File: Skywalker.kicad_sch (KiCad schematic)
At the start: 53 parts

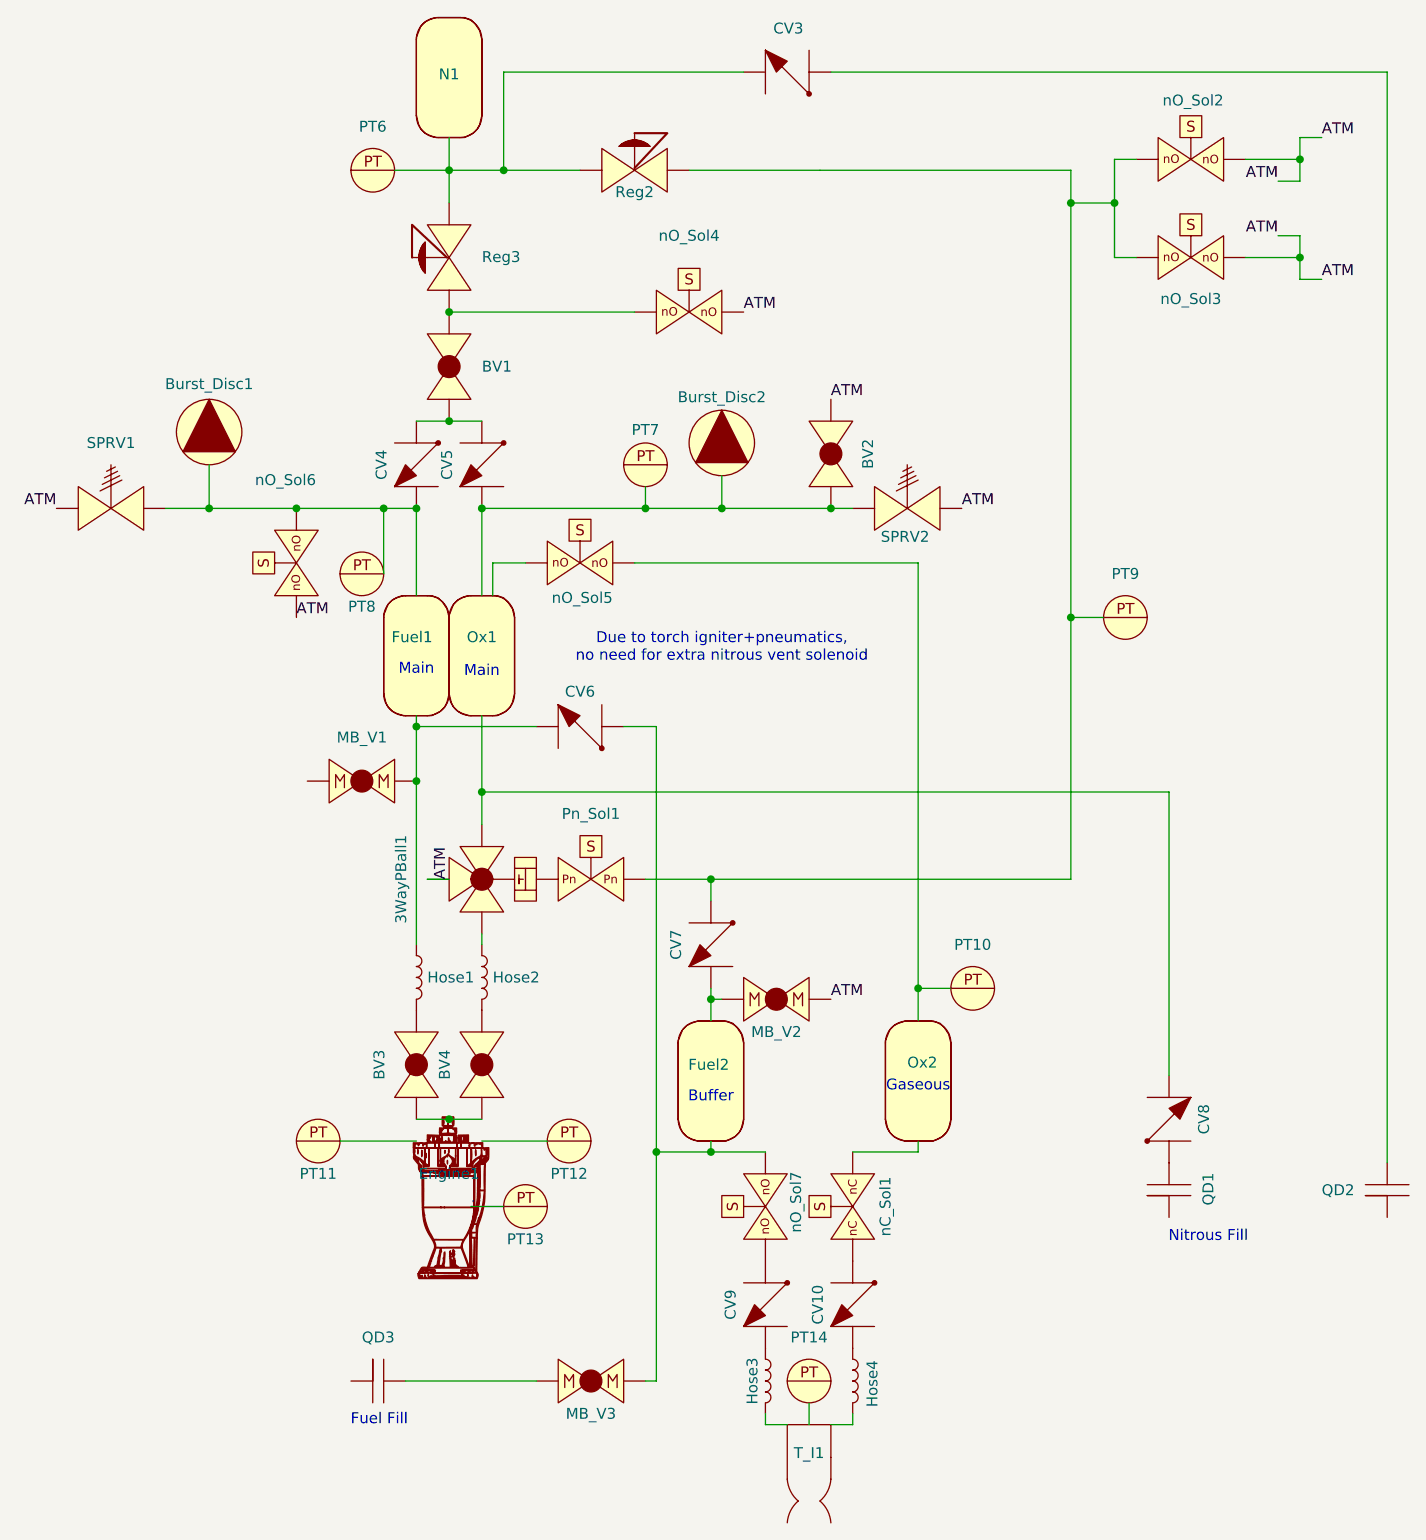
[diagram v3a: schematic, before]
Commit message: Added Igniter + Hopper Engine test
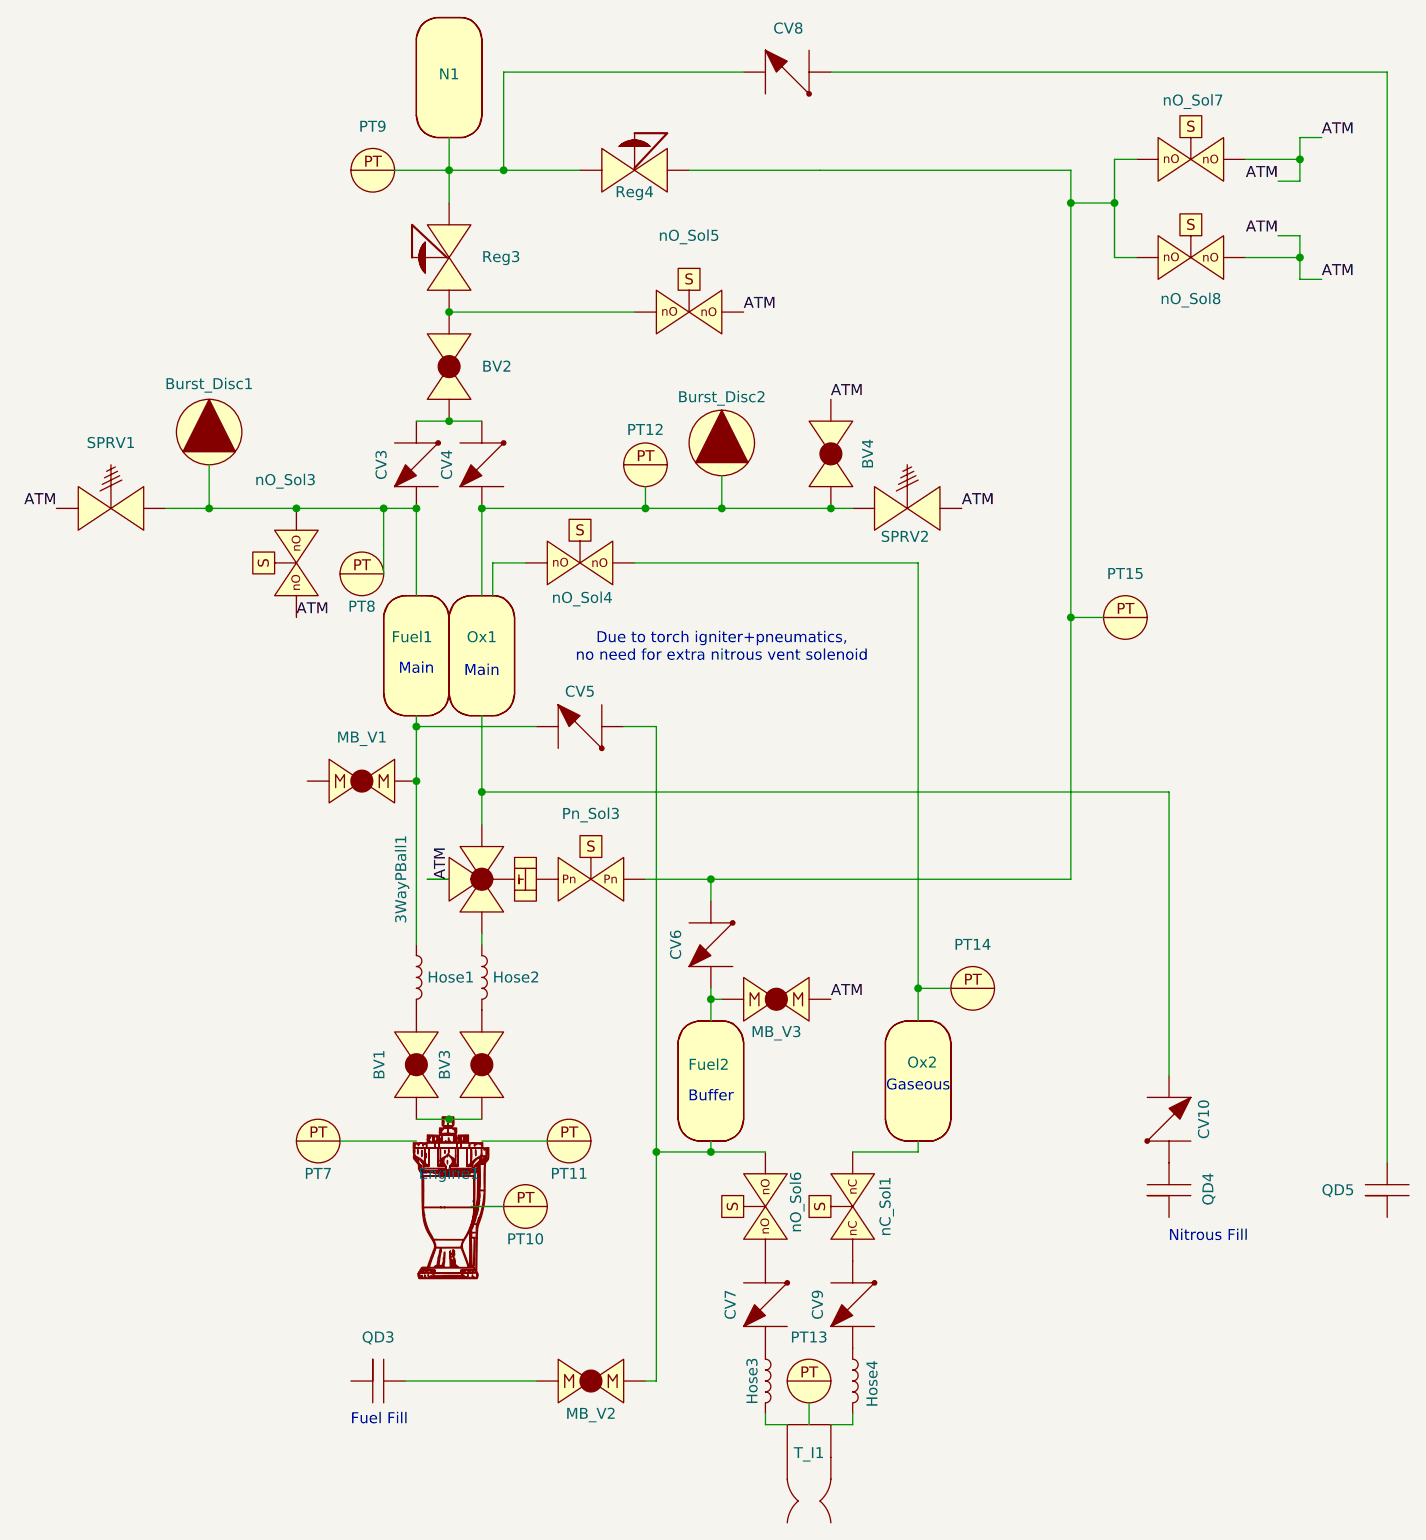
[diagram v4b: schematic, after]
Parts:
- renumbered BV3 to BV1, BV1 to BV2, BV4 to BV3, BV2 to BV4, CV8 to CV10, CV4 to CV3, CV5 to CV4, CV6 to CV5, CV7 to CV6, CV9 to CV7, CV3 to CV8, CV10 to CV9, MB_V3 to MB_V2, MB_V2 to MB_V3, PT13 to PT10, PT12 to PT11, PT7 to PT12, PT14 to PT13, PT10 to PT14, PT9 to PT15, PT11 to PT7, PT6 to PT9, Pn_Sol1 to Pn_Sol3, QD1 to QD4, QD2 to QD5, Reg2 to Reg4, nO_Sol6 to nO_Sol3, nO_Sol5 to nO_Sol4, nO_Sol4 to nO_Sol5, nO_Sol7 to nO_Sol6, nO_Sol2 to nO_Sol7, nO_Sol3 to nO_Sol8
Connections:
- net at N1.: now also CV8., PT9., Reg3., Reg4.
- net at Engine1.: now also PT7.; no longer PT11.
- net at PT7.: no longer Engine1.
- net at CV9.: now also Hose4.1; no longer nC_Sol1.
- net at QD4.: now also CV10.
- new net: CV6., PT15., Pn_Sol3., Reg4., nO_Sol7., nO_Sol8.
- new net: CV6., Fuel2., MB_V3.
- new net: Engine1., PT11.
- new net: BV1., BV3., Engine1.
- new net: CV5., Fuel2., MB_V2., nO_Sol6.
- new net: CV9., nC_Sol1.
- new net: Burst_Disc1., CV3., Fuel1., PT8., SPRV1., nO_Sol3.
- new net: BV2., CV3., CV4.
- new net: Ox2., PT14., nO_Sol4.
- new net: 3WayPBall1., CV10., Ox1.
- new net: BV4., Burst_Disc2., CV4., Ox1., PT12., SPRV2.
- now unconnected: Burst_Disc1., Burst_Disc2., PT12., PT14., PT15., PT8., PT9.

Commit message: overwrite
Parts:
- renumbered PT10 to Chamber, PT7 to Fuel_Inj, PT13 to Igniter, PT9 to N2_Hose, PT11 to Ox_Inj
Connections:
- net at N1.: now also CV8., N2_Hose., Reg3., Reg4.
- net at Engine1.: now also Fuel_Inj.; no longer Ox_Inj.
- net at Fuel_Inj.: no longer Engine1.
- net at CV9.: now also Hose4.1; no longer nC_Sol1.
- net N2_GSS: now reaches QD5.
- net OX_GSS: now reaches QD4.
- new net: CV6., PT15., Pn_Sol3., Reg4., nO_Sol7., nO_Sol8.
- new net: CV6., Fuel2., MB_V3.
- new net: Engine1., Ox_Inj.
- new net: BV1., BV3., Engine1.
- new net: CV5., Fuel2., MB_V2., nO_Sol6.
- new net: CV9., nC_Sol1.
- new net: Burst_Disc1., CV3., Fuel1., PT8., SPRV1., nO_Sol3.
- new net: BV2., CV3., CV4.
- new net: Ox2., PT14., nO_Sol4.
- new net: 3WayPBall1., CV10., Ox1.
- new net: BV4., Burst_Disc2., CV4., Ox1., PT12., SPRV2.
- now unconnected: Burst_Disc1., Burst_Disc2., N2_Hose., PT12., PT14., PT15., PT8.
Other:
- note removed: "Nitrous Fill"
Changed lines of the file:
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@@
+	(wire
+		(pts
+			(xy 147.32 161.29) (xy 147.32 156.21)
+		)
+		(stroke
+			(width 0)
+			(type default)
+		)
+	)
 	(wire
 		(pts
@@
 	(wire
 		(pts
+			(xy 172.72 161.29) (xy 172.72 156.21)
+		)
+		(stroke
+			(width 0)
+			(type default)
+		)
+	)
+	(wire
+		(pts
 			(xy 140.97 33.02) (xy 140.97 38.1)
 		)
@@
 		)
 	)
-	(text "Nitrous Fill"
-		(exclude_from_sim no)
-		(at 151.892 158.496 0)
-		(effects
-			(font
-				(size 1.27 1.27)
-			)
-		)
-	)
 	(text "Gaseous"
 		(exclude_from_sim no)
@@
 	(label "ATM"
 		(at 17.78 73.66 180)
+		(fields_autoplaced yes)
 		(effects
 			(font
@@
 	(label "ATM"
 		(at 160.02 41.91 180)
+		(fields_autoplaced yes)
 		(effects
 			(font
@@
 	(label "ATM"
 		(at 165.1 46.99 0)
+		(fields_autoplaced yes)
 		(effects
 			(font
@@
 	(label "ATM"
 		(at 123.19 73.66 0)
+		(fields_autoplaced yes)
 		(effects
 			(font
@@
 	(label "."
 		(at 66.04 154.94 0)
+		(fields_autoplaced yes)
 		(effects
 			(font
@@
 	(label "ATM"
 		(at 107.95 130.81 0)
+		(fields_autoplaced yes)
 		(effects
 			(font
@@
 		)
 	)
-	(label "ATM"
-		(at 165.1 30.48 0)
+	(label "N2_GSS"
+		(at 172.72 161.29 180)
+		(fields_autoplaced yes)
 		(effects
 			(font
 				(size 1.27 1.27)
 			)
+			(justify right bottom)
+		)
+	)
+	(label "ATM"
+		(at 165.1 30.48 0)
+		(fields_autoplaced yes)
+		(effects
+			(font
+				(size 1.27 1.27)
+			)
 			(justify left bottom)
 		)
@@
 	(label "."
 		(at 105.41 180.34 0)
+		(fields_autoplaced yes)
 		(effects
 			(font
@@
 		)
 	)
+	(label "OX_GSS"
+		(at 147.32 161.29 0)
+		(fields_autoplaced yes)
+		(effects
+			(font
+				(size 1.27 1.27)
+			)
+			(justify left bottom)
+		)
+	)
 	(label "."
 		(at 68.58 83.82 0)
+		(fields_autoplaced yes)
 		(effects
 			(font
@@
 	(label "ATM"
 		(at 97.79 50.8 0)
+		(fields_autoplaced yes)
 		(effects
 			(font
@@
 	(label "ATM"
 		(at 63.5 116.84 90)
+		(fields_autoplaced yes)
 		(effects
 			(font
@@
 	(label "ATM"
 		(at 45.72 86.36 0)
+		(fields_autoplaced yes)
 		(effects
 			(font
@@
 	(label "ATM"
 		(at 107.95 60.96 0)
+		(fields_autoplaced yes)
 		(effects
 			(font
@@
 	(label "ATM"
 		(at 160.02 35.56 180)
+		(fields_autoplaced yes)
 		(effects
 			(font
@@
 	)
 	(symbol
+		(lib_name "PID_symbols:Pressure_Transducer")
 		(lib_id "PID_symbols:Pressure_Transducer")
 		(at 72.39 154.94 0)
@@
 		(on_board yes)
 		(dnp no)
-		(property "Reference" "PT10"
+		(property "Reference" "Chamber"
 			(at 72.39 158.75 0)
 			(effects
@@
 			(project "P_IDs"
 				(path "/045f1f05-3134-4b6d-91b6-463031104f1e/8ff5724e-b29b-49c2-a1fa-190081404476"
-					(reference "PT10")
+					(reference "Chamber")
 					(unit 1)
 				)
@@
 	)
 	(symbol
+		(lib_name "PID_symbols:Pressure_Transducer")
 		(lib_id "PID_symbols:Pressure_Transducer")
 		(at 77.47 147.32 0)
@@
 		(on_board yes)
 		(dnp no)
-		(property "Reference" "PT11"
+		(property "Reference" "Ox_Inj"
 			(at 77.47 151.13 0)
 			(effects
@@
 			(project "P_IDs"
 				(path "/045f1f05-3134-4b6d-91b6-463031104f1e/8ff5724e-b29b-49c2-a1fa-190081404476"
-					(reference "PT11")
+					(reference "Ox_Inj")
 					(unit 1)
 				)
@@
 	)
 	(symbol
+		(lib_name "PID_symbols:Pressure_Transducer")
 		(lib_id "PID_symbols:Pressure_Transducer")
 		(at 48.26 147.32 0)
@@
 		(on_board yes)
 		(dnp no)
-		(property "Reference" "PT7"
+		(property "Reference" "Fuel_Inj"
 			(at 48.26 151.13 0)
 			(effects
@@
 			(project "P_IDs"
 				(path "/045f1f05-3134-4b6d-91b6-463031104f1e/8ff5724e-b29b-49c2-a1fa-190081404476"
-					(reference "PT7")
+					(reference "Fuel_Inj")
 					(unit 1)
 				)
@@
 	)
 	(symbol
+		(lib_name "PID_symbols:Pressure_Transducer")
 		(lib_id "PID_symbols:Pressure_Transducer")
 		(at 105.41 175.26 0)
@@
 		(dnp no)
 		(fields_autoplaced yes)
-		(property "Reference" "PT13"
+		(property "Reference" "Igniter"
 			(at 105.41 170.18 0)
 			(effects
@@
 			(project ""
 				(path "/045f1f05-3134-4b6d-91b6-463031104f1e/8ff5724e-b29b-49c2-a1fa-190081404476"
-					(reference "PT13")
+					(reference "Igniter")
 					(unit 1)
 				)
@@
 	)
 	(symbol
+		(lib_name "PID_symbols:Pressure_Transducer")
 		(lib_id "PID_symbols:Pressure_Transducer")
 		(at 54.61 34.29 0)
@@
 		(dnp no)
 		(fields_autoplaced yes)
-		(property "Reference" "PT9"
+		(property "Reference" "N2_Hose"
 			(at 54.61 29.21 0)
 			(effects
@@
 			(project ""
 				(path "/045f1f05-3134-4b6d-91b6-463031104f1e/8ff5724e-b29b-49c2-a1fa-190081404476"
-					(reference "PT9")
-					(unit 1)
-				)
+					(reference "N2_Hose")
+					(unit 1)
+				)

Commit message: no message
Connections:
- net at N1.: now also CV8., N2_Hose., Reg3., Reg4.
- net at Engine1.: now also Fuel_Inj.; no longer Ox_Inj.
- net at Fuel_Inj.: no longer Engine1.
- net at CV9.: now also Hose4.1; no longer nC_Sol1.
- new net: CV6., PT15., Pn_Sol3., Reg4., nO_Sol7., nO_Sol8.
- new net: CV6., Fuel2., MB_V3.
- new net: Engine1., Ox_Inj.
- new net: BV1., BV3., Engine1.
- new net: CV5., Fuel2., MB_V2., nO_Sol6.
- new net: CV9., nC_Sol1.
- new net: Burst_Disc1., CV3., Fuel1., PT8., SPRV1., nO_Sol3.
- new net: BV2., CV3., CV4.
- new net: Ox2., PT14., nO_Sol4.
- new net: 3WayPBall1., CV10., Ox1.
- new net: BV4., Burst_Disc2., CV4., Ox1., PT12., SPRV2.
- now unconnected: Burst_Disc1., Burst_Disc2., N2_Hose., PT12., PT14., PT15., PT8.
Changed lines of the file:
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@@
 	)
 	(symbol
-		(lib_name "PID_symbols:Pressure_Transducer")
 		(lib_id "PID_symbols:Pressure_Transducer")
 		(at 72.39 154.94 0)
@@
 	)
 	(symbol
-		(lib_name "PID_symbols:Pressure_Transducer")
 		(lib_id "PID_symbols:Pressure_Transducer")
 		(at 77.47 147.32 0)
@@
 	)
 	(symbol
-		(lib_name "PID_symbols:Pressure_Transducer")
 		(lib_id "PID_symbols:Pressure_Transducer")
 		(at 48.26 147.32 0)
@@
 	)
 	(symbol
-		(lib_name "PID_symbols:Pressure_Transducer")
 		(lib_id "PID_symbols:Pressure_Transducer")
 		(at 105.41 175.26 0)
@@
 	)
 	(symbol
-		(lib_name "PID_symbols:Pressure_Transducer")
 		(lib_id "PID_symbols:Pressure_Transducer")
 		(at 54.61 34.29 0)
@@
 		)
 	)
+	(sheet_instances
+		(path "/"
+			(page "1")
+		)
+	)

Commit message: no message
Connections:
- net at N1.: now also CV8., N2_Hose., Reg3., Reg4.
- net at Engine1.: now also Fuel_Inj.; no longer Ox_Inj.
- net at Fuel_Inj.: no longer Engine1.
- net at CV9.: now also Hose4.1; no longer nC_Sol1.
- new net: CV6., PT15., Pn_Sol3., Reg4., nO_Sol7., nO_Sol8.
- new net: CV6., Fuel2., MB_V3.
- new net: Engine1., Ox_Inj.
- new net: BV1., BV3., Engine1.
- new net: CV5., Fuel2., MB_V2., nO_Sol6.
- new net: CV9., nC_Sol1.
- new net: Burst_Disc1., CV3., Fuel1., PT8., SPRV1., nO_Sol3.
- new net: BV2., CV3., CV4.
- new net: Ox2., PT14., nO_Sol4.
- new net: 3WayPBall1., CV10., Ox1.
- new net: BV4., Burst_Disc2., CV4., Ox1., PT12., SPRV2.
- now unconnected: Burst_Disc1., Burst_Disc2., N2_Hose., PT12., PT14., PT15., PT8.
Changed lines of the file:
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@@
 	)
 	(symbol
+		(lib_name "PID_symbols:Pressure_Transducer")
 		(lib_id "PID_symbols:Pressure_Transducer")
 		(at 72.39 154.94 0)
@@
 	)
 	(symbol
+		(lib_name "PID_symbols:Pressure_Transducer")
 		(lib_id "PID_symbols:Pressure_Transducer")
 		(at 77.47 147.32 0)
@@
 	)
 	(symbol
+		(lib_name "PID_symbols:Pressure_Transducer")
 		(lib_id "PID_symbols:Pressure_Transducer")
 		(at 48.26 147.32 0)
@@
 	)
 	(symbol
+		(lib_name "PID_symbols:Pressure_Transducer")
 		(lib_id "PID_symbols:Pressure_Transducer")
 		(at 105.41 175.26 0)
@@
 	)
 	(symbol
+		(lib_name "PID_symbols:Pressure_Transducer")
 		(lib_id "PID_symbols:Pressure_Transducer")
 		(at 54.61 34.29 0)
@@
 		)
 	)
-	(sheet_instances
-		(path "/"
-			(page "1")
-		)
-	)

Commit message: no message
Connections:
- net at N1.: now also CV8., N2_Hose., Reg3., Reg4.
- net at Engine1.: now also Fuel_Inj.; no longer Ox_Inj.
- net at Fuel_Inj.: no longer Engine1.
- net at CV9.: now also Hose4.1; no longer nC_Sol1.
- new net: CV6., PT15., Pn_Sol3., Reg4., nO_Sol7., nO_Sol8.
- new net: CV6., Fuel2., MB_V3.
- new net: Engine1., Ox_Inj.
- new net: BV1., BV3., Engine1.
- new net: CV5., Fuel2., MB_V2., nO_Sol6.
- new net: CV9., nC_Sol1.
- new net: Burst_Disc1., CV3., Fuel1., PT8., SPRV1., nO_Sol3.
- new net: BV2., CV3., CV4.
- new net: Ox2., PT14., nO_Sol4.
- new net: 3WayPBall1., CV10., Ox1.
- new net: BV4., Burst_Disc2., CV4., Ox1., PT12., SPRV2.
- now unconnected: Burst_Disc1., Burst_Disc2., N2_Hose., PT12., PT14., PT15., PT8.
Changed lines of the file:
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@@
 	)
 	(symbol
-		(lib_name "PID_symbols:Pressure_Transducer")
 		(lib_id "PID_symbols:Pressure_Transducer")
 		(at 72.39 154.94 0)
@@
 	)
 	(symbol
-		(lib_name "PID_symbols:Pressure_Transducer")
 		(lib_id "PID_symbols:Pressure_Transducer")
 		(at 77.47 147.32 0)
@@
 	)
 	(symbol
-		(lib_name "PID_symbols:Pressure_Transducer")
 		(lib_id "PID_symbols:Pressure_Transducer")
 		(at 48.26 147.32 0)
@@
 	)
 	(symbol
-		(lib_name "PID_symbols:Pressure_Transducer")
 		(lib_id "PID_symbols:Pressure_Transducer")
 		(at 105.41 175.26 0)
@@
 	)
 	(symbol
-		(lib_name "PID_symbols:Pressure_Transducer")
 		(lib_id "PID_symbols:Pressure_Transducer")
 		(at 54.61 34.29 0)
@@
 	)
 	(symbol
+		(lib_name "PID_symbols:MBallValve")
 		(lib_id "PID_symbols:MBallValve")
 		(at 101.6 130.81 0)
+		(mirror y)
 		(unit 1)
 		(exclude_from_sim no)
@@
 		)
 	)
+	(sheet_instances
+		(path "/"
+			(page "1")
+		)
+	)
